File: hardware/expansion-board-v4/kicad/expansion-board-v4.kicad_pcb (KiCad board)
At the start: 6 copper layers, 100 x 62 mm, 174 parts, among them J1 PinHeader_2x20_P2.54mm_Vertic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, J2 U.FL_Hirose_U.FL-R-SMT-1_Vert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, J4 USB_C_Receptacle_HRO_TYPE-C-3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, J5 U.FL_Hirose_U.FL-R-SMT-1_Vert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, J6 U.FL_Hirose_U.FL-R-SMT-1_Vert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, J7 U.FL_Hirose_U.FL-R-SMT-1_Vert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, J8 U.FL_Hirose_U.FL-R-SMT-1_Vert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, J9 MX1.25WT-2P, Q2 SOT-23, Q3 SOT-23, Q4 SOT-23, Q5 SOT-23, SW2 SolderJumper-2_P1.3mm_Open_Pa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, U1 SOT-23-5, U10 QFN-48-1EP_7x7mm_P0.5mm_EP5.1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, U11 DFN-8-1EP_2x2mm_P0.5mm_EP0.86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, U12 SOT-363_SC-70-6, U14 MSOP-8_3x3mm_P0.65mm, U15 SOT-23-6, U16 SOT-363_SC-70-6, U17 SOT-363_SC-70-6, U18 SOIC-10_3.9x4.9mm_P1mm, U19 QFN-24-1EP_4x4mm_P0.5mm_EP2.6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, U2 SOT-23-5, U20 TSOT-23-6, U3 SOT-23-5, U4 BNO085_LGA-28, U5 BMP388_LGA-10, U6 LGA-16_3x3mm_P0.5mm, U7 ATGM336H_LCC-18, U8 QFN-56-1EP_7x7mm_P0.4mm_EP3.2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, U9 SOIC-8_5.3x5.3mm_P1.27mm, Y1 Crystal_SMD_3225-4Pin_3.2x2.5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, Y2 Crystal_SMD_3225-4Pin_3.2x2.5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, Y3 Crystal_SMD_3215-2Pin_3.2x1.5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

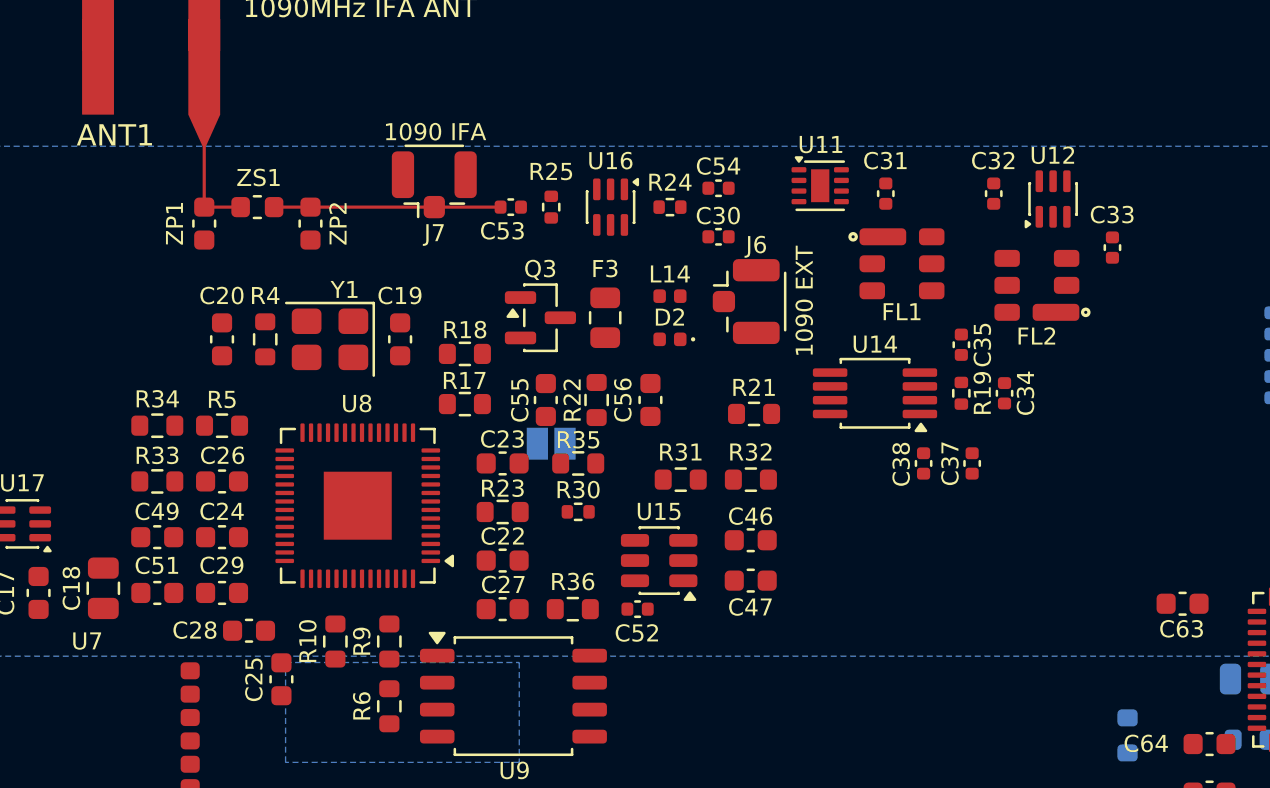
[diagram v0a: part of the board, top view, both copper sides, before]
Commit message: fix(v4): Data Slicer 三条支路按「滤波贴负载」归位
判据：串联电阻是阻抗分界线。电阻之前由源的输出阻抗决定（几十欧），走多长
都不怕；电阻之后源阻抗变成电阻值本身（10k/100k），那一段就是天线。并联
电容则是「高阻段到此为止」的那个点。所以 RC 滤波的两个件都要贴负载。

三条支路的高阻段（串阻 → 并容）：
  FAST    R31→C46   3.32mm  （本来就对）
  LEVEL   R33→C47  28.37 → 1.98mm
  RSSI    R35→C51  19.21 → 2.63mm

长走线相应挪到了低阻段上，均无害：
  C49→R33 26.34mm  LEVEL_BIAS 被 C49 的 100nF 交流接地
  源→R35  28.69mm  AD8313 的缓冲输出，低阻

R34+C49 保持贴 U8 不动：TL_PWM 是 PWM 方波、本身是噪声源，越早积分成直流
越好，不能让方波横穿整块板。

同轮用户还微调了 U11/U12/C32/C33/C54（1090 主链，各 0.5~2mm）。

DRC 6 条 0 error、未连接 292、parity 0。
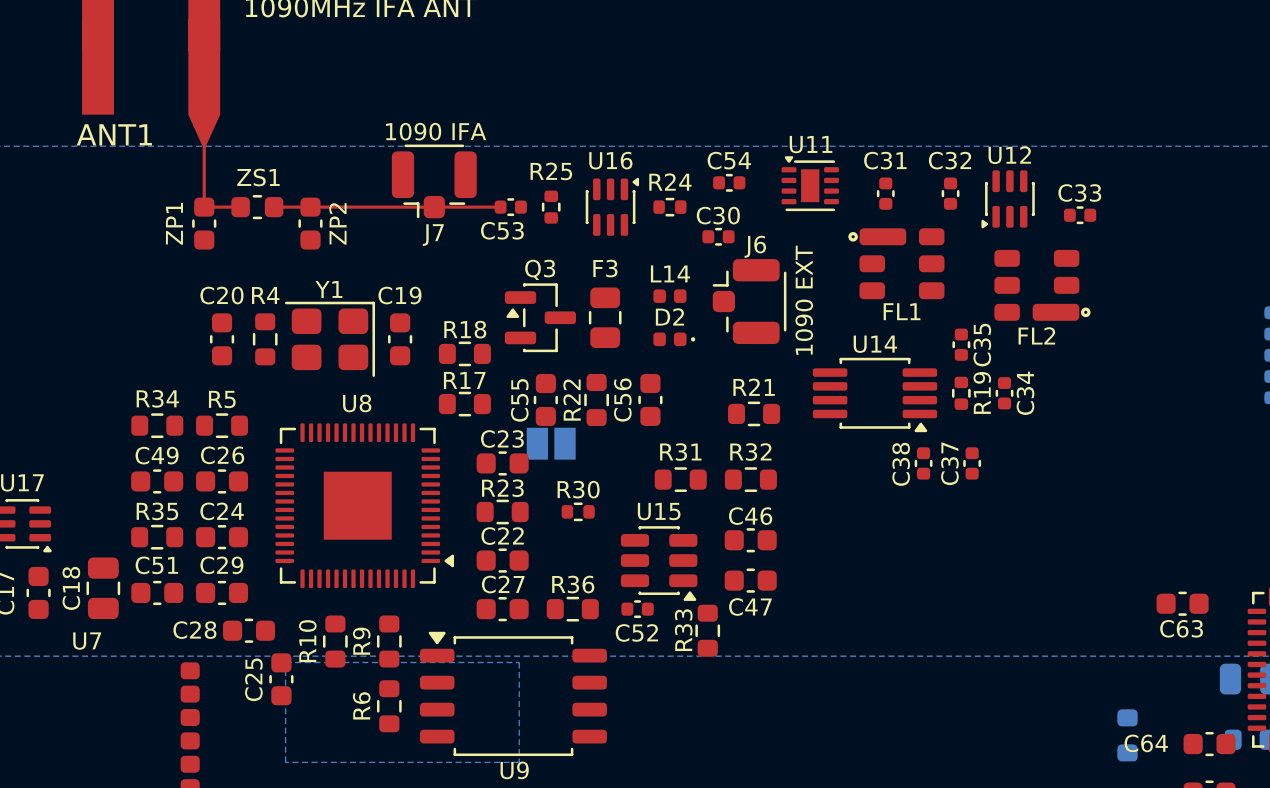
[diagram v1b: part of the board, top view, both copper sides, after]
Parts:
- moved R33 26.8 mm to (102.9, 82.8), turned to 90 degrees
- moved R35 20.1 mm to (77.0, 78.4), turned to 0 degrees
- moved C49 2.62 mm to (77.0, 75.8)
- moved C33 2.16 mm to (120.4, 63.2), turned to 0 degrees
- moved U12 2.03 mm to (117.1, 62.5)
- moved C32 2.03 mm to (114.3, 62.2)
- moved C54 0.57 mm to (103.9, 61.7)
- moved U11 0.47 mm to (107.7, 61.9)
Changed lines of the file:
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@@
 	(footprint "C_0402_1005Metric"
 		(layer "F.Cu")
-		(at 103.378 61.976)
+		(at 103.886 61.722)
 		(descr "Capacitor SMD 0402 (1005 Metric), square (rectangular) end terminal, IPC-7351 nominal, (Body size source: IPC-SM-782 page 76, https://www.pcb-3d.com/wordpress/wp-content/uploads/ipc-sm-782a_amendment_1_and_2.pdf)")
 		(tags "capacitor")
@@
 		(tags "resistor")
 		(property "Reference" "R36"
-			(at 0 1.27 0)
+			(at 0 1.129428 0)
 			(layer "F.SilkS")
 			(effects
@@
 	(footprint "R_0603_1608Metric"
 		(layer "F.Cu")
-		(at 96.774 74.93 180)
+		(at 76.957819 78.401333)
 		(descr "Resistor SMD 0603 (1608 Metric), square (rectangular) end terminal, IPC-7351 nominal, (Body size source: IPC-SM-782 page 72, https://www.pcb-3d.com/wordpress/wp-content/uploads/ipc-sm-782a_amendment_1_and_2.pdf)")
 		(tags "resistor")
 		(property "Reference" "R35"
-			(at -0.008527 1.087144 180)
+			(at 0.004181 -1.185333 0)
 			(layer "F.SilkS")
 			(effects
@@
 		(duplicate_pad_numbers_are_jumpers no)
 		(fp_line
-			(start -0.237258 0.5225)
-			(end 0.237258 0.5225)
+			(start -0.237258 -0.5225)
+			(end 0.237258 -0.5225)
 			(stroke
 				(width 0.12)
@@
 		)
 		(fp_line
-			(start -0.237258 -0.5225)
-			(end 0.237258 -0.5225)
+			(start -0.237258 0.5225)
+			(end 0.237258 0.5225)
 			(stroke
 				(width 0.12)
@@
 		)
 		(pad "1" smd roundrect
-			(at -0.825 0 180)
+			(at -0.825 0)
 			(size 0.8 0.95)
 			(layers "F.Cu" "F.Mask" "F.Paste")
@@
 		)
 		(pad "2" smd roundrect
-			(at 0.825 0 180)
+			(at 0.825 0)
 			(size 0.8 0.95)
 			(layers "F.Cu" "F.Mask" "F.Paste")
@@
 	(footprint "C_0603_1608Metric"
 		(layer "F.Cu")
-		(at 76.957819 78.401333 180)
+		(at 76.957819 75.776667 180)
 		(descr "Capacitor SMD 0603 (1608 Metric), square (rectangular) end terminal, IPC-7351 nominal, (Body size source: IPC-SM-782 page 76, https://www.pcb-3d.com/wordpress/wp-content/uploads/ipc-sm-782a_amendment_1_and_2.pdf)")
 		(tags "capacitor")
@@
 		(descr "SMD3225/4, Crystal, 3.2x2.5mm package, SMD, http://www.txccrystal.com/images/pdf/7m-accuracy.pdf")
 		(property "Reference" "Y1"
-			(at -0.712 2.318 0)
+			(at 0 2.318 0)
 			(layer "F.SilkS")
 			(effects
@@
 	(footprint "C_0402_1005Metric"
 		(layer "F.Cu")
-		(at 121.92 64.77 -90)
+		(at 120.396 63.246)
 		(descr "Capacitor SMD 0402 (1005 Metric), square (rectangular) end terminal, IPC-7351 nominal, (Body size source: IPC-SM-782 page 76, https://www.pcb-3d.com/wordpress/wp-content/uploads/ipc-sm-782a_amendment_1_and_2.pdf)")
 		(tags "capacitor")
 		(property "Reference" "C33"
-			(at -1.524 0 180)
+			(at 0 -1.016 180)
 			(layer "F.SilkS")
 			(effects
@@
 		)
 		(property "Value" "C_0402_1005Metric"
-			(at 0 1.16 90)
+			(at 0 1.16 0)
 			(layer "F.Fab")
 			(effects
@@
 		)
 		(property "Datasheet" ""
-			(at 0 0 90)
+			(at 0 0 0)
 			(layer "F.Fab")
 			(hide yes)
@@
 		)
 		(property "Description" ""
-			(at 0 0 90)
+			(at 0 0 0)
 			(layer "F.Fab")
 			(hide yes)
@@
 		)
 		(property "KiLib_Generator" "SMD_2terminal_chip_molded"
-			(at 0 0 90)
+			(at 0 0 0)
 			(layer "F.SilkS")
 			(hide yes)
@@
 		(duplicate_pad_numbers_are_jumpers no)
 		(fp_line
-			(start -0.107836 0.36)
-			(end 0.107836 0.36)
+			(start -0.107836 -0.36)
+			(end 0.107836 -0.36)
 			(stroke
 				(width 0.12)
@@
 		)
 		(fp_line
-			(start -0.107836 -0.36)
-			(end 0.107836 -0.36)
+			(start -0.107836 0.36)
+			(end 0.107836 0.36)
 			(stroke
 				(width 0.12)
@@
 		)
 		(fp_text user "${REFERENCE}"
-			(at 0 0 90)
+			(at 0 0 0)
 			(layer "F.Fab")
 			(effects
@@
 		)
 		(pad "1" smd roundrect
-			(at -0.48 0 270)
+			(at -0.48 0)
 			(size 0.56 0.62)
 			(layers "F.Cu" "F.Mask" "F.Paste")
@@
 		)
 		(pad "2" smd roundrect
-			(at 0.48 0 270)
+			(at 0.48 0)
 			(size 0.56 0.62)
 			(layers "F.Cu" "F.Mask" "F.Paste")
@@
 	(footprint "C_0402_1005Metric"
 		(layer "F.Cu")
-		(at 116.332 62.23 90)
+		(at 114.3 62.23 90)
 		(descr "Capacitor SMD 0402 (1005 Metric), square (rectangular) end terminal, IPC-7351 nominal, (Body size source: IPC-SM-782 page 76, https://www.pcb-3d.com/wordpress/wp-content/uploads/ipc-sm-782a_amendment_1_and_2.pdf)")
 		(tags "capacitor")
@@
 	(footprint "SOT-363_SC-70-6"
 		(layer "F.Cu")
-		(at 119.126 62.484 90)
+		(at 117.094 62.484 90)
 		(descr "SOT, 6 Pin (https://home.jeita.or.jp/tsc/std-pdf/ED-7500A.pdf#page=170, JEDEC MO-203, variant AB, https://www.jedec.org/document_search?search_api_views_fulltext=MO-203)")
 		(tags "SOT TO_SOT_SMD SC-88 SOT-363 SC-70-6 US6 UMT6 S-Mini6 TSSOP6")
@@
 	(footprint "DFN-8-1EP_2x2mm_P0.5mm_EP0.86x1.55mm"
 		(layer "F.Cu")
-		(at 108.165 61.858)
+		(at 107.696 61.858)
 		(descr "DFN, 8 Pin (https://www.diodes.com/assets/Datasheets/PAM2841.pdf)")
 		(tags "DFN NoLead")
@@
 	(footprint "R_0603_1608Metric"
 		(layer "F.Cu")
-		(at 76.962 75.776667 180)
+		(at 102.87 82.804 90)
 		(descr "Resistor SMD 0603 (1608 Metric), square (rectangular) end terminal, IPC-7351 nominal, (Body size source: IPC-SM-782 page 72, https://www.pcb-3d.com/wordpress/wp-content/uploads/ipc-sm-782a_amendment_1_and_2.pdf)")
 		(tags "resistor")
 		(property "Reference" "R33"
-			(at 0 1.199224 0)
+			(at 0.015451 -1.100231 90)
 			(layer "F.SilkS")
 			(effects
@@
 		)
 		(property "Value" "R_0603_1608Metric"
-			(at 0 1.43 0)
+			(at 0 1.43 90)
 			(layer "F.Fab")
 			(effects
@@
 		)
 		(property "Datasheet" ""
-			(at 0 0 0)
+			(at 0 0 90)
 			(layer "F.Fab")
 			(hide yes)
@@
 		)
 		(property "Description" ""
-			(at 0 0 0)
+			(at 0 0 90)
 			(layer "F.Fab")
 			(hide yes)
@@
 		)
 		(property "KiLib_Generator" "SMD_2terminal_chip_molded"
-			(at 0 0 0)
+			(at 0 0 90)
 			(layer "F.SilkS")
 			(hide yes)
@@
 		(duplicate_pad_numbers_are_jumpers no)
 		(fp_line
-			(start -0.237258 0.5225)
-			(end 0.237258 0.5225)
+			(start -0.237258 -0.5225)
+			(end 0.237258 -0.5225)
 			(stroke
 				(width 0.12)
@@
 		)
 		(fp_line
-			(start -0.237258 -0.5225)
-			(end 0.237258 -0.5225)
+			(start -0.237258 0.5225)
+			(end 0.237258 0.5225)
 			(stroke
 				(width 0.12)
@@
 		)
 		(fp_text user "${REFERENCE}"
-			(at 0 0 0)
+			(at 0 0 90)
 			(layer "F.Fab")
 			(effects
@@
 		)
 		(pad "1" smd roundrect
-			(at -0.825 0 180)
+			(at -0.825 0 90)
 			(size 0.8 0.95)
 			(layers "F.Cu" "F.Mask" "F.Paste")
@@
 		)
 		(pad "2" smd roundrect
-			(at 0.825 0 180)
+			(at 0.825 0 90)
 			(size 0.8 0.95)
 			(layers "F.Cu" "F.Mask" "F.Paste")

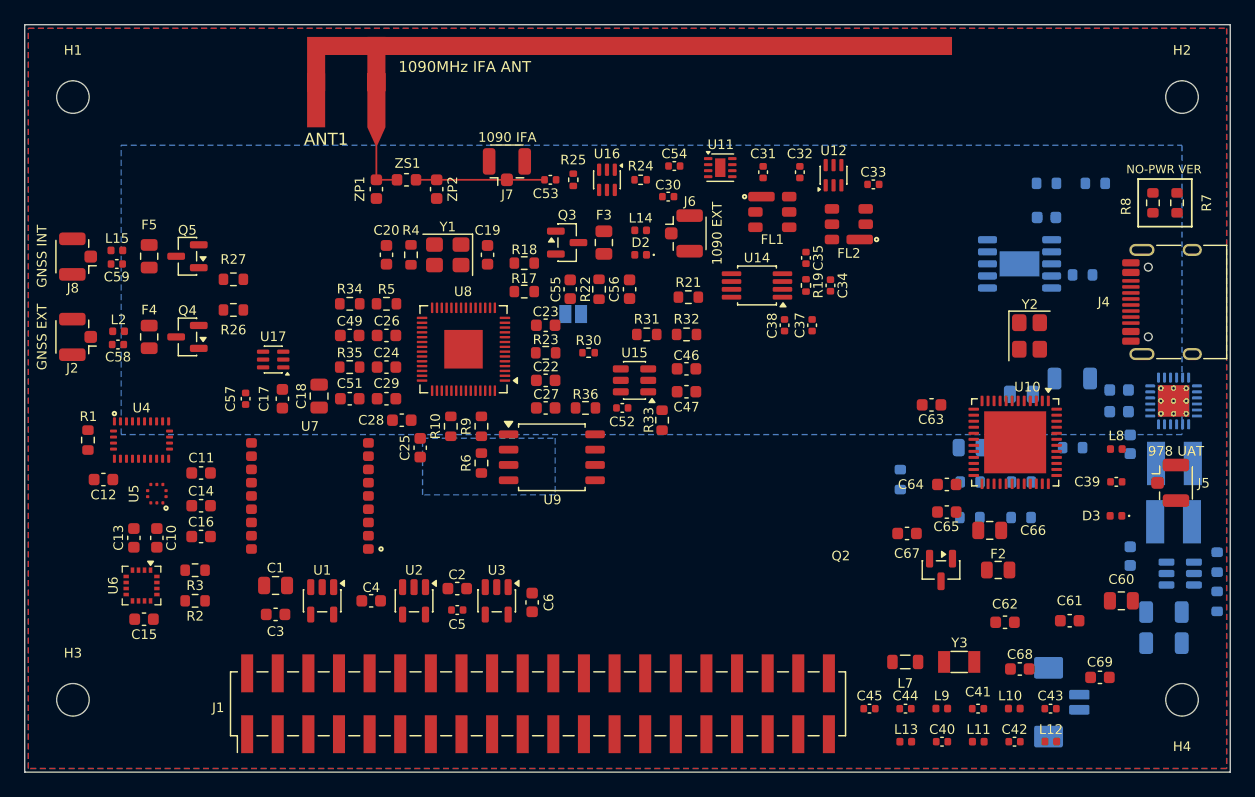
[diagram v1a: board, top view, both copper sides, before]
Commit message: chore(v4): 固化 978/U10 区重排（34 件），三份数据全部同步
用户手工把整个 978 区从板子东侧搬到中南部并重排：
U10 (132.160,84.642) → (104.513,91.968) rot270→180，J5 → (124.333,108.332)，
balun 六件、梯形五件、晶振两组、DCDC、四颗去耦全部跟随。

射频节点收紧（MST）：
  SUBG_RFP   8.15 → 6.09mm      SUBG_N3   7.80 → 6.05mm
  SUBG_N4   10.16 → 3.60mm      SUBG_N5   7.24 → 3.73mm
对地支路（并联电容离本节点最近件）：
  C41 4.06 → 2.03    C42 8.13 → 2.29    C43 5.80 → 2.29    C44 2.03 → 1.19mm
关键单点：
  L7(DCDC 电感) ↔ SUBG_SW  18.68 → 2.13mm
  C63/C64/C65/C66 四颗 3V3_DIG 去耦从 19~25mm 收到 2.8~4.7mm，
  且正好一边一颗，对应 U10 四条边上的四个 3V3_DIG 脚
  VDDR 三颗顺序修正：C62(100nF) 2.15 < C61(100nF) 4.29 < C60(22uF) 7.38mm

主路径 U10.RF_P → L9 → L11 → L12 → C39 → L8 → J5 全程单调，无折返。

固化三份（缺一份就复现不出来）：
  PLACEMENT.py  174 元件 / 174 位号  回读逐条比对，不一致 0，最大残差 0.0007mm
  SILK.json     16 条板级文字（'978 UAT' 跟着 J5 移到南边，护栏拦下并已更新）
  ROUTES.json   本轮未布线，无变化

DRC 6 条 0 error、未连接 292、parity 0、IFA 走廊 5 项测试通过。
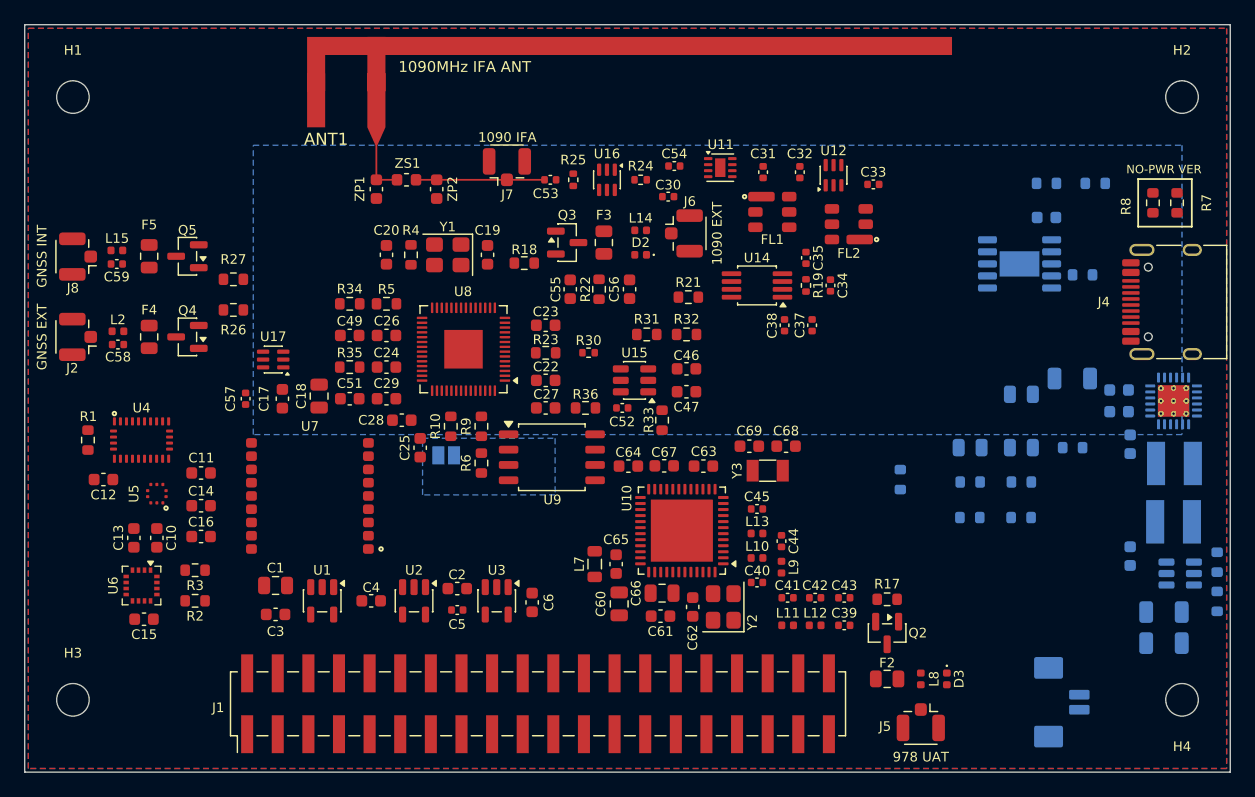
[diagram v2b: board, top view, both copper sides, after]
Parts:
- moved C60 41.7 mm to (99.3, 98.0), turned to 90 degrees
- moved R17 39.5 mm to (121.5, 97.7), turned to 0 degrees
- moved C69 34.8 mm to (110.1, 85.0), turned to 180 degrees
- moved C61 33.9 mm to (102.7, 99.1), turned to 180 degrees
- moved Y2 33.9 mm to (108.0, 98.3), turned to 90 degrees
- moved J5 29.4 mm to (124.3, 108.3), turned to -90 degrees
- moved U10 28.6 mm to (104.5, 92.0), turned to 180 degrees
- moved C65 27.8 mm to (99.1, 94.7), turned to -90 degrees
- moved C66 27.7 mm to (102.9, 97.2), turned to 180 degrees
- moved L7 27.0 mm to (97.3, 94.7), turned to -90 degrees
- moved C68 26.8 mm to (113.2, 85.0)
- moved C64 26.5 mm to (100.1, 86.6), turned to 180 degrees
- moved C62 25.9 mm to (105.4, 98.3), turned to -90 degrees
- moved C39 25.5 mm to (118.0, 99.8)
- moved L8 25.0 mm to (124.3, 104.3), turned to -90 degrees
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
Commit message: feat(v4): 「面」纳入固化数据；修好 gen_pcb.py 的四处陈旧，首次实现完全复现
## 起因

把 27 个电源件从 B 面整组镜像搬到 F 面后发现：PLACEMENT.py 的元组是
(位号, x, y, rot)，**不记面**。谁在 B 面由 gen_pcb.py 里一张写死的 BACKSIDE
集合决定，而那张表还停在搬迁前——跑一次 gen_pcb.py 就会把这 27 个件全翻回
B 面，而 PLACEMENT 里的 x 已是镜像后的坐标，翻回去是一团乱麻。

**固化数据缺一个维度，平时看不出来，一重建就丢**——与 SILK.json 同一类问题。

## 改动

1. PLACEMENT.py 元组加第 5 个字段「面」('F'/'B')，export_placement.py 导出时写入
2. gen_pcb.py 新增 _is_back()：固化数据优先，BACKSIDE 降级为新元件兜底；
   没有面记录而按 BACKSIDE 翻的会打印警告，提示跑 export_placement.py
3. 三处解包适配变长元组（PINNED / _FIXED / integrate_ifa_v4 的 POS），
   一律改用切片，以后再加字段不会炸

## 顺带修好 gen_pcb.py 四处让它跑不起来的陈旧

- 区域互斥断言**与自己的注释自相矛盾**：注释写「冻结件不受区域约束」，
  代码却拿区域断言所有 PINNED（全是冻结件）。用户把 J2 挪进 LEFT_EDGE 区后
  卡死半个月。改为只检查真正走装箱器的新元件
- 区域成员表里积了已删除的位号（D1/SW1/TP1–7/U13/R20），漏进装箱器直接
  KeyError: 'D1'，报错信息看不出根因。改为在源头过滤并打印跳过清单
- 安装孔 H1~H4 单独 Add、不在 FPS 里，位号丝印还原循环覆盖不到——
  往返比对时它们是仅有的 4 个差异，其中 H4 被手工挪过 7.5mm 会丢
- integrate_ifa_v4.py 里 J7 坐标写死 96.773（V3.5 时代值），2026-08-26
  评审把 J7 挪到 90.000 后该脚本一直跑不了。改为读 PLACEMENT.py，
  真正该守的「J7 在 π 网络主线上」改成断言 y 与 ZP2 一致

## 验证

副本上跑 gen_pcb.py（退出码 0，本会话首次），与实板逐件比对 174 件：
位置 0 / 旋转 0 / **面 0** / 位号丝印 0 差异，最大残差 0.0005mm — 完全复现。

## 同轮固化

用户手工重排电源区 27 件 + RT1 移回 B 面(120.904, 82.042)。
两块电源岛按负载包络重画（详见上一提交），B.Cu GND 由 4 块碎铜合并为 1 块。
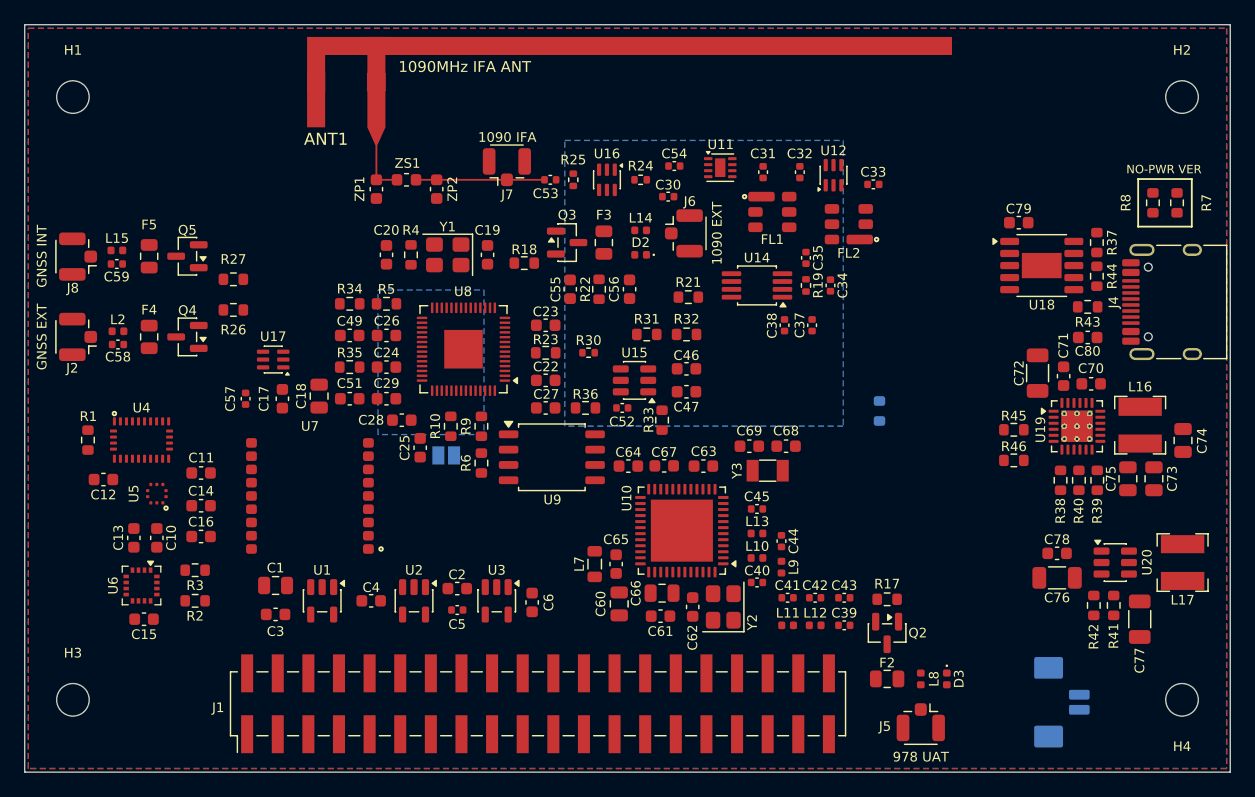
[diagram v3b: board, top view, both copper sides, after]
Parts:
- C70, C71, C72, C73, C74, C75, C76, C77, C78, C79, C80, L16, L17, R37, R38, R39, R40, R41, R42, R43, R44, R45, R46, U18, U19, U20: moved to F.Cu
- moved C74 17.7 mm to (146.1, 84.5), turned to 90 degrees
- moved C73 13.0 mm to (143.7, 87.7), turned to -90 degrees
- moved R43 10.8 mm to (138.2, 73.4), turned to 180 degrees
- moved R39 10.5 mm to (139.0, 87.8), turned to 90 degrees
- moved R42 10.2 mm to (138.7, 98.2)
- moved C76 9.31 mm to (135.6, 95.9), turned to 180 degrees
- moved R41 9.30 mm to (140.3, 98.2)
- moved C75 9.21 mm to (141.5, 87.7), turned to -90 degrees
- moved U19 8.28 mm to (137.3, 83.3), turned to 0 degrees
- moved R45 8.14 mm to (132.1, 83.6), turned to 180 degrees
- moved R44 7.71 mm to (138.9, 70.9), turned to 90 degrees
- moved C78 6.07 mm to (135.6, 93.9), turned to 180 degrees
- moved C70 5.96 mm to (138.5, 79.8), turned to 0 degrees
- moved RT1 5.95 mm to (120.9, 82.0)
- moved U20 5.46 mm to (140.5, 94.6), turned to 0 degrees
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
